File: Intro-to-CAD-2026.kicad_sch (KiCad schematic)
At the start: 6 parts

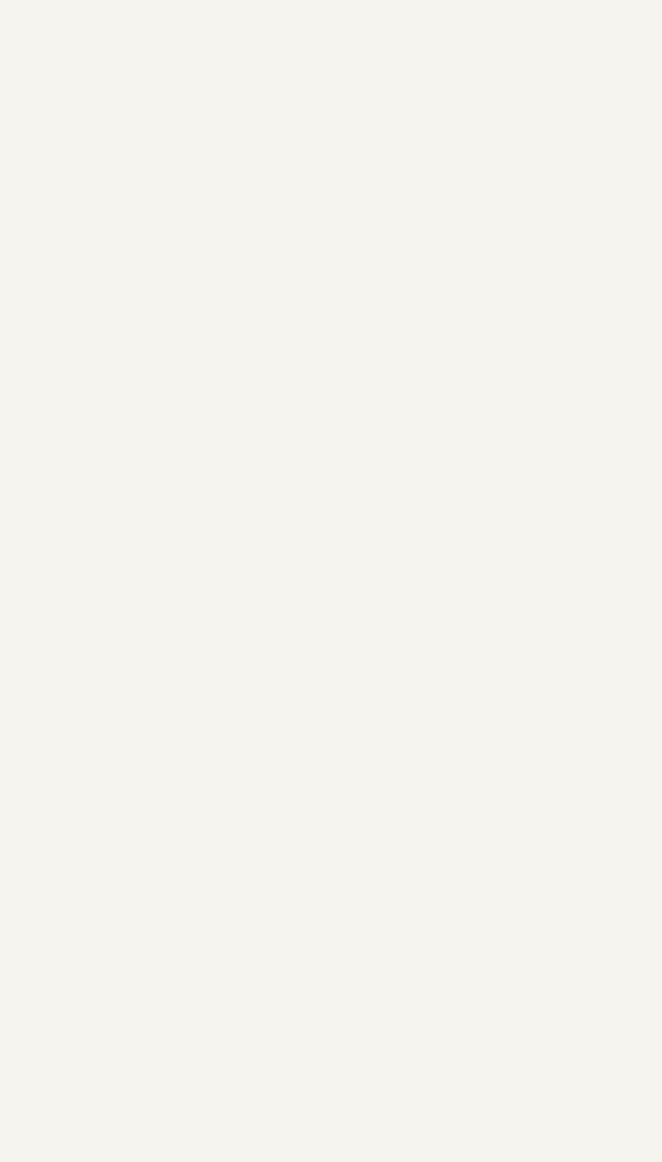
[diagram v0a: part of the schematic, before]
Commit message: Added module schematics.
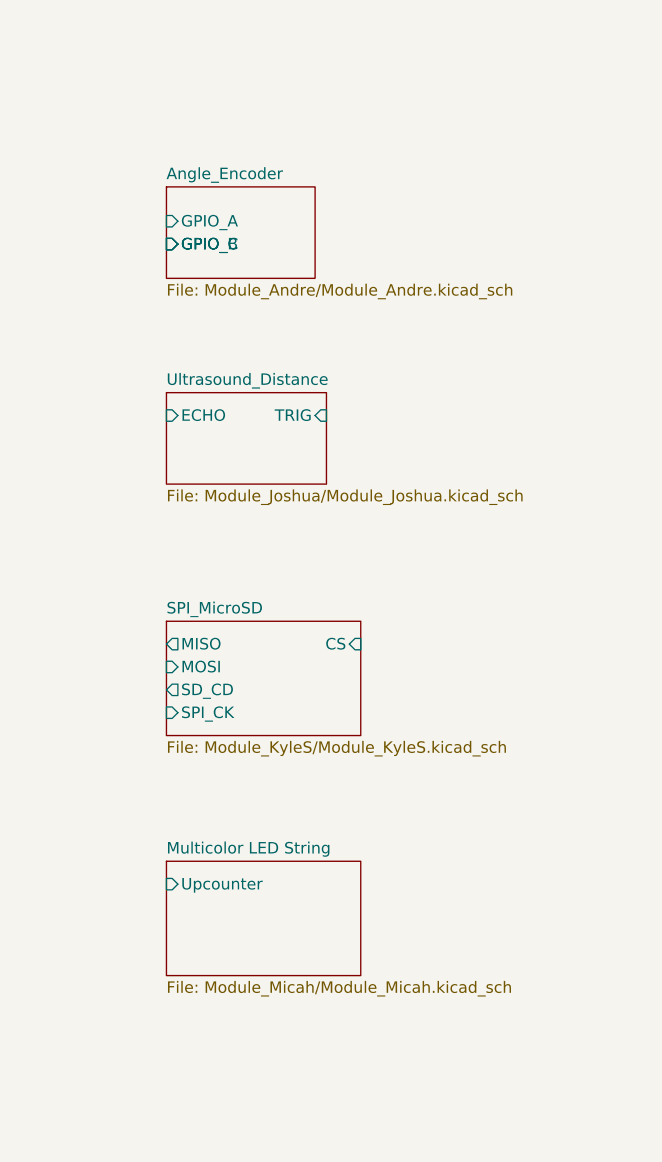
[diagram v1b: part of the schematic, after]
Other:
- added sheet Angle_Encoder (Module_Andre/Module_Andre.kicad_sch)
- added sheet Multicolor LED String (Module_Micah/Module_Micah.kicad_sch)
- added sheet SPI_MicroSD (Module_KyleS/Module_KyleS.kicad_sch)
- added sheet Ultrasound_Distance (Module_Joshua/Module_Joshua.kicad_sch)

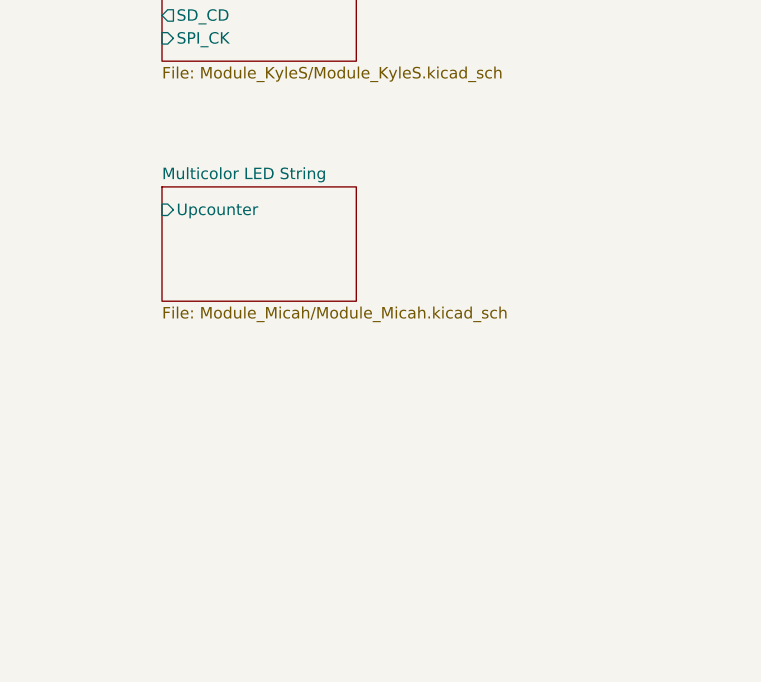
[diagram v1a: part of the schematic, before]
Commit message: Imported Student Parts
Not using Project Instances yet.
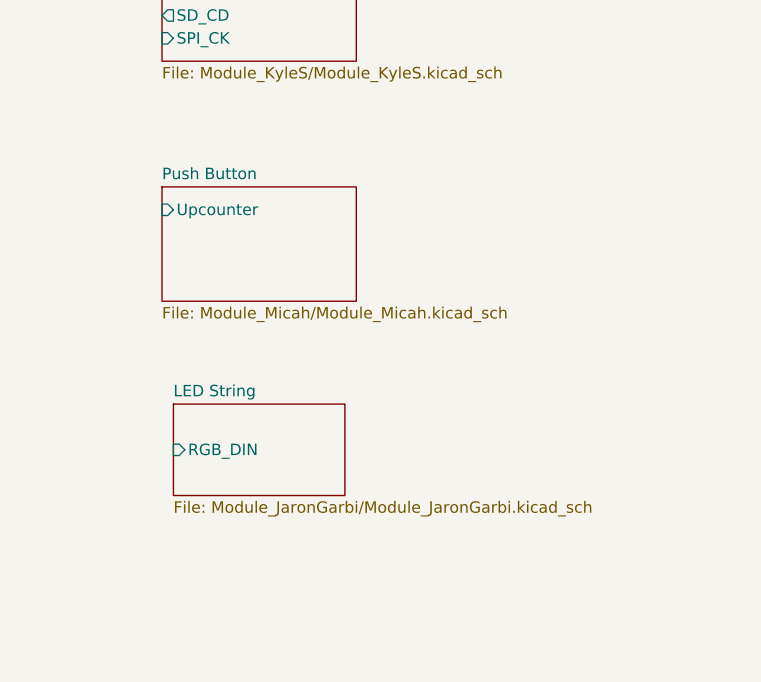
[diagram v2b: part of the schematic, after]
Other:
- sheet Multicolor LED String renamed Push Button
- added sheet LED String (Module_JaronGarbi/Module_JaronGarbi.kicad_sch)
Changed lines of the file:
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@@
+	)
+	(sheet
+		(at 125.73 138.43)
+		(size 19.05 10.16)
+		(exclude_from_sim no)
+		(in_bom yes)
+		(on_board yes)
+		(dnp no)
+		(fields_autoplaced yes)
+		(stroke
+			(width 0.1524)
+			(type solid)
+		)
+		(fill
+			(color 0 0 0 0.0000)
+		)
+		(property "Sheetname" "LED String"
+			(at 125.73 137.7184 0)
+			(effects
+				(font
+					(size 1.27 1.27)
+				)
+				(justify left bottom)
+			)
+		)
+		(property "Sheetfile" "Module_JaronGarbi/Module_JaronGarbi.kicad_sch"
+			(at 125.73 149.1746 0)
+			(effects
+				(font
+					(size 1.27 1.27)
+				)
+				(justify left top)
+			)
+		)
+		(pin "RGB_DIN" input
+			(at 125.73 143.51 180)
+			(effects
+				(font
+					(size 1.27 1.27)
+				)
+				(justify left)
+			)
+		)
+		(instances
+			(project "Intro-to-CAD-2026"
+				(path "/c12dc015-e6cb-468c-8de4-269c3106de0e"
+					(page "13")
+				)
+			)
+		)
 	)
 	(sheet
@@
 			(color 0 0 0 0.0000)
 		)
-		(property "Sheetname" "Multicolor LED String"
+		(property "Sheetname" "Push Button"
 			(at 124.46 113.5884 0)
 			(effects

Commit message: Going to school.
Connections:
- no-connect marks 19 -> 13
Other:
- added sheet OLED (oled.kicad_sch)
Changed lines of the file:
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@@
 	)
 	(no_connect
-		(at 57.15 27.94)
-	)
-	(no_connect
-		(at 57.15 25.4)
-	)
-	(no_connect
 		(at 86.36 44.45)
 	)
 	(no_connect
-		(at 57.15 35.56)
-	)
-	(no_connect
-		(at 57.15 30.48)
-	)
-	(no_connect
 		(at 86.36 52.07)
 	)
 	(no_connect
-		(at 57.15 33.02)
+		(at 146.05 92.71)
 	)
 	(no_connect
@@
 	)
 	(no_connect
-		(at 57.15 40.64)
-	)
-	(no_connect
 		(at 86.36 39.37)
 	)
@@
 	)
 	(no_connect
-		(at 57.15 38.1)
-	)
-	(no_connect
 		(at 86.36 41.91)
 	)
@@
 		)
 	)
+	(label "CS"
+		(at 57.15 27.94 180)
+		(effects
+			(font
+				(size 1.27 1.27)
+			)
+			(justify right bottom)
+		)
+	)
 	(label "OSC_SCL"
 		(at 25.4 58.42 180)
@@
 		)
 	)
+	(label "CS"
+		(at 124.46 95.25 180)
+		(effects
+			(font
+				(size 1.27 1.27)
+			)
+			(justify right bottom)
+		)
+	)
 	(label "Q_CLK"
 		(at 62.23 120.65 180)
@@
 		)
 	)
+	(label "MISO"
+		(at 124.46 90.17 180)
+		(effects
+			(font
+				(size 1.27 1.27)
+			)
+			(justify right bottom)
+		)
+	)
 	(label "MCLK"
 		(at 57.15 45.72 180)
@@
 		)
 	)
+	(label "MOSI"
+		(at 57.15 33.02 180)
+		(effects
+			(font
+				(size 1.27 1.27)
+			)
+			(justify right bottom)
+		)
+	)
 	(label "I_CLK"
 		(at 82.55 158.75 0)
@@
 		)
 	)
+	(label "SPI_CK"
+		(at 57.15 30.48 180)
+		(effects
+			(font
+				(size 1.27 1.27)
+			)
+			(justify right bottom)
+		)
+	)
 	(label "SDA"
 		(at 39.37 72.39 180)
@@
 		)
 	)
+	(label "MOSI"
+		(at 124.46 92.71 180)
+		(effects
+			(font
+				(size 1.27 1.27)
+			)
+			(justify right bottom)
+		)
+	)
 	(label "SDIN"
 		(at 57.15 43.18 180)
@@
 		)
 	)
+	(label "SPI_CK"
+		(at 124.46 97.79 180)
+		(effects
+			(font
+				(size 1.27 1.27)
+			)
+			(justify right bottom)
+		)
+	)
 	(label "OSC_SCL"
 		(at 62.23 165.1 180)
@@
 		)
 	)
+	(label "MISO"
+		(at 57.15 25.4 180)
+		(effects
+			(font
+				(size 1.27 1.27)
+			)
+			(justify right bottom)
+		)
+	)
 	(label "LRCK"
 		(at 62.23 138.43 180)
@@
 		)
 		(pin "CS" input
-			(at 146.05 90.17 0)
+			(at 124.46 95.25 180)
 			(effects
 				(font
 					(size 1.27 1.27)
 				)
-				(justify right)
+				(justify left)
 			)
 		)
@@
 		)
 		(pin "SD_CD" output
-			(at 124.46 95.25 180)
+			(at 146.05 92.71 0)
 			(effects
 				(font
 					(size 1.27 1.27)
 				)
-				(justify left)
+				(justify right)
 			)
 		)
@@
 		)
 		(pin "TRIG" input
-			(at 142.24 64.77 0)
+			(at 124.46 67.31 180)
 			(effects
 				(font
 					(size 1.27 1.27)
 				)
-				(justify right)
+				(justify left)
 			)
 		)
@@
 				)
 			)
+		)
+	)
+	(sheet
+		(at 173.355 91.44)
+		(size 24.765 13.97)
+		(exclude_from_sim no)
+		(in_bom yes)
+		(on_board yes)
+		(dnp no)
+		(fields_autoplaced yes)
+		(stroke
+			(width 0.1524)
+			(type solid)
+		)
+		(fill
+			(color 0 0 0 0.0000)
+		)
+		(property "Sheetname" "OLED"
+			(at 173.355 90.7284 0)
+			(effects
+				(font
+					(size 1.27 1.27)
+				)
+				(justify left bottom)
+			)
+		)
+		(property "Sheetfile" "oled.kicad_sch"
+			(at 173.355 105.9946 0)
+			(effects
+				(font
+					(size 1.27 1.27)
+				)
+				(justify left top)
+			)
+		)
+		(instances
+			(project "Intro-to-CAD-2026"
+				(path "/c12dc015-e6cb-468c-8de4-269c3106de0e"
+					(page "14")
+				)
+			)

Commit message: No Errors No Warnings
Some were excluded.
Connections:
- no-connect marks 13 -> 7
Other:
- sheet OLED ports: added SCL, SDA; removed none
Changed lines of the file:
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@@
 	)
 	(no_connect
-		(at 86.36 59.69)
-	)
-	(no_connect
-		(at 86.36 49.53)
+		(at 57.15 40.64)
 	)
 	(no_connect
@@
 	)
 	(no_connect
-		(at 86.36 52.07)
-	)
-	(no_connect
-		(at 146.05 92.71)
-	)
-	(no_connect
-		(at 86.36 54.61)
-	)
-	(no_connect
 		(at 82.55 162.56)
 	)
 	(no_connect
-		(at 86.36 46.99)
-	)
-	(no_connect
 		(at 86.36 39.37)
 	)
@@
 	)
 	(no_connect
-		(at 86.36 57.15)
-	)
-	(no_connect
 		(at 86.36 31.75)
 	)
@@
 		)
 	)
+	(label "SW_C"
+		(at 124.46 46.99 180)
+		(effects
+			(font
+				(size 1.27 1.27)
+			)
+			(justify right bottom)
+		)
+	)
 	(label "CS"
 		(at 57.15 27.94 180)
@@
 		)
 	)
+	(label "SCL"
+		(at 124.46 166.37 180)
+		(effects
+			(font
+				(size 1.27 1.27)
+			)
+			(justify right bottom)
+		)
+	)
+	(label "ANG_A"
+		(at 124.46 41.91 180)
+		(effects
+			(font
+				(size 1.27 1.27)
+			)
+			(justify right bottom)
+		)
+	)
 	(label "OSC_SCL"
 		(at 25.4 58.42 180)
@@
 		)
 	)
+	(label "SDA"
+		(at 124.46 163.83 180)
+		(effects
+			(font
+				(size 1.27 1.27)
+			)
+			(justify right bottom)
+		)
+	)
 	(label "I_CLK"
 		(at 62.23 118.11 180)
@@
 		)
 	)
+	(label "RGB_DIN"
+		(at 86.36 46.99 0)
+		(effects
+			(font
+				(size 1.27 1.27)
+			)
+			(justify left bottom)
+		)
+	)
+	(label "ANG_B"
+		(at 124.46 44.45 180)
+		(effects
+			(font
+				(size 1.27 1.27)
+			)
+			(justify right bottom)
+		)
+	)
 	(label "DATA"
 		(at 57.15 60.96 180)
@@
 		)
 	)
+	(label "TRIG"
+		(at 86.36 54.61 0)
+		(effects
+			(font
+				(size 1.27 1.27)
+			)
+			(justify left bottom)
+		)
+	)
 	(label "CS"
 		(at 124.46 95.25 180)
@@
 		)
 	)
+	(label "SW_C"
+		(at 57.15 38.1 180)
+		(effects
+			(font
+				(size 1.27 1.27)
+			)
+			(justify right bottom)
+		)
+	)
 	(label "Q"
 		(at 62.23 184.15 180)
@@
 		)
 	)
+	(label "ANG_A"
+		(at 86.36 57.15 0)
+		(effects
+			(font
+				(size 1.27 1.27)
+			)
+			(justify left bottom)
+		)
+	)
+	(label "ANG_B"
+		(at 86.36 59.69 0)
+		(effects
+			(font
+				(size 1.27 1.27)
+			)
+			(justify left bottom)
+		)
+	)
 	(label "MOSI"
 		(at 57.15 33.02 180)
@@
 		)
 	)
+	(label "ECHO"
+		(at 124.46 64.77 180)
+		(effects
+			(font
+				(size 1.27 1.27)
+			)
+			(justify right bottom)
+		)
+	)
 	(label "I_CLK"
 		(at 82.55 158.75 0)
@@
 		)
 	)
+	(label "RGB_DIN"
+		(at 125.73 143.51 180)
+		(effects
+			(font
+				(size 1.27 1.27)
+			)
+			(justify right bottom)
+		)
+	)
 	(label "MOSI"
 		(at 124.46 92.71 180)
@@
 		)
 	)
+	(label "BTN"
+		(at 86.36 49.53 0)
+		(effects
+			(font
+				(size 1.27 1.27)
+			)
+			(justify left bottom)
+		)
+	)
 	(label "LRCK"
 		(at 57.15 48.26 180)
@@
 		)
 	)
+	(label "SD_CD"
+		(at 57.15 35.56 180)
+		(effects
+			(font
+				(size 1.27 1.27)
+			)
+			(justify right bottom)
+		)
+	)
 	(label "I"
 		(at 62.23 181.61 180)
@@
 		)
 	)
+	(label "SD_CD"
+		(at 146.05 92.71 0)
+		(effects
+			(font
+				(size 1.27 1.27)
+			)
+			(justify left bottom)
+		)
+	)
 	(label "MISO"
 		(at 57.15 25.4 180)
@@
 		)
 	)
+	(label "BTN"
+		(at 124.46 119.38 180)
+		(effects
+			(font
+				(size 1.27 1.27)
+			)
+			(justify right bottom)
+		)
+	)
+	(label "TRIG"
+		(at 124.46 67.31 180)
+		(effects
+			(font
+				(size 1.27 1.27)
+			)
+			(justify right bottom)
+		)
+	)
 	(label "BCK"
 		(at 82.55 185.42 0)
@@
 		)
 	)
+	(label "ECHO"
+		(at 86.36 52.07 0)
+		(effects
+			(font
+				(size 1.27 1.27)
+			)
+			(justify left bottom)
+		)
+	)
 	(label "MD1"
 		(at 57.15 53.34 180)
@@
 			)
 		)
-		(pin "GPIO_A" input
-			(at 124.46 43.18 180)
+		(pin "GPIO_A" output
+			(at 124.46 41.91 180)
 			(effects
 				(font
@@
 			)
 		)
-		(pin "GPIO_B" input
-			(at 124.46 45.72 180)
+		(pin "GPIO_B" output
+			(at 124.46 44.45 180)
 			(effects
 				(font
@@
 			)
 		)
-		(pin "GPIO_C" input
-			(at 124.46 45.72 180)
+		(pin "GPIO_C" output
+			(at 124.46 46.99 180)
 			(effects
 				(font
@@
 			)
 		)
-		(pin "ECHO" input
-			(at 124.46 64.77 180)
+		(pin "TRIG" input
+			(at 124.46 67.31 180)
 			(effects
 				(font
@@
 			)
 		)
-		(pin "TRIG" input
-			(at 124.46 67.31 180)
+		(pin "ECHO" output
+			(at 124.46 64.77 180)
 			(effects
 				(font
@@
 			)
 		)
-		(pin "LRCK" input
-			(at 62.23 138.43 180)
+		(pin "SDIN" input
+			(at 62.23 146.05 180)
 			(effects
 				(font
@@
 			)
 		)
-		(pin "MCLK" input
-			(at 62.23 140.97 180)
+		(pin "LRCK" output
+			(at 62.23 138.43 180)
 			(effects
 				(font
@@
 			)
 		)
-		(pin "SCLK" input
-			(at 62.23 143.51 180)
+		(pin "MCLK" output
+			(at 62.23 140.97 180)
 			(effects
 				(font
@@
 			)
 		)
-		(pin "SDIN" input
-			(at 62.23 146.05 180)
+		(pin "SCLK" input
+			(at 62.23 143.51 180)
 			(effects
 				(font
@@
 	)
 	(sheet
-		(at 173.355 91.44)
-		(size 24.765 13.97)
+		(at 124.46 157.48)
+		(size 24.13 13.97)
 		(exclude_from_sim no)
 		(in_bom yes)
@@
 		)
 		(property "Sheetname" "OLED"
-			(at 173.355 90.7284 0)
+			(at 124.46 156.7684 0)
 			(effects
 				(font
@@
 		)
 		(property "Sheetfile" "oled.kicad_sch"
-			(at 173.355 105.9946 0)
+			(at 124.46 172.0346 0)
 			(effects
 				(font
@@
 			)
 		)
+		(pin "SCL" input
+			(at 124.46 166.37 180)
+			(effects
+				(font
+					(size 1.27 1.27)
+				)
+				(justify left)
+			)
+		)
+		(pin "SDA" input
+			(at 124.46 163.83 180)
+			(effects
+				(font
+					(size 1.27 1.27)
+				)
+				(justify left)
+			)
+		)
 		(instances
 			(project "Intro-to-CAD-2026"
@@
 			)
 		)
-		(pin "Upcounter" input
-			(at 124.46 116.84 180)
+		(pin "Upcounter" output
+			(at 124.46 119.38 180)
 			(effects
 				(font

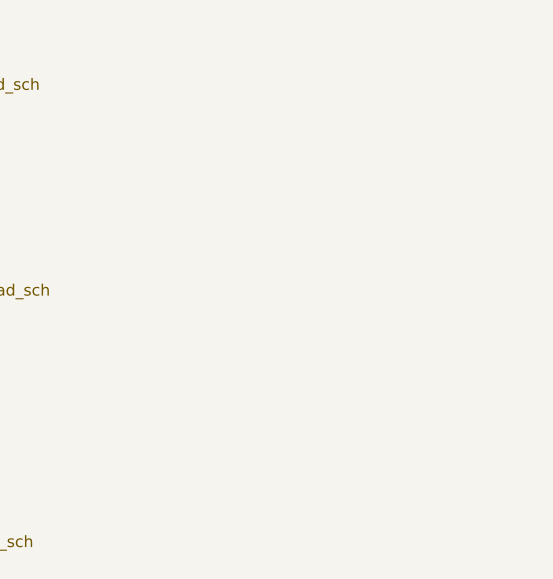
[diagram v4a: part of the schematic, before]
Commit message: Adding TC118S
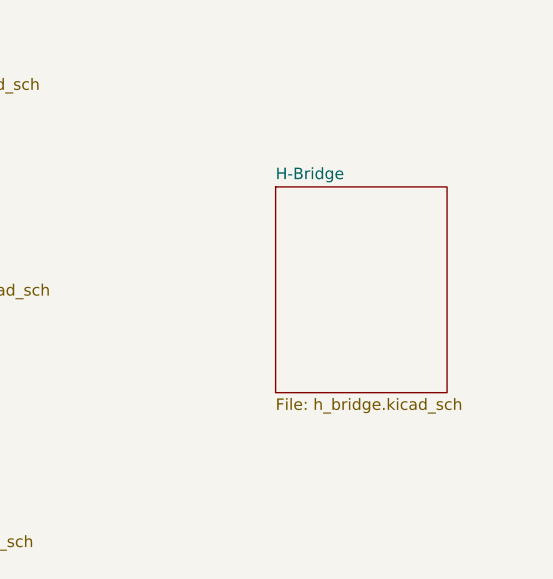
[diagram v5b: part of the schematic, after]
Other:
- added sheet H-Bridge (h_bridge.kicad_sch)
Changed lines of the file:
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@@
+	)
+	(sheet
+		(at 189.23 62.23)
+		(size 19.05 22.86)
+		(exclude_from_sim no)
+		(in_bom yes)
+		(on_board yes)
+		(dnp no)
+		(fields_autoplaced yes)
+		(stroke
+			(width 0.1524)
+			(type solid)
+		)
+		(fill
+			(color 0 0 0 0.0000)
+		)
+		(property "Sheetname" "H-Bridge"
+			(at 189.23 61.5184 0)
+			(effects
+				(font
+					(size 1.27 1.27)
+				)
+				(justify left bottom)
+			)
+		)
+		(property "Sheetfile" "h_bridge.kicad_sch"
+			(at 189.23 85.6746 0)
+			(effects
+				(font
+					(size 1.27 1.27)
+				)
+				(justify left top)
+			)
+		)
+		(instances
+			(project "Intro-to-CAD-2026"
+				(path "/c12dc015-e6cb-468c-8de4-269c3106de0e"
+					(page "15")
+				)
+			)
+		)
 	)
 	(sheet

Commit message: Added H-Bridge PCB Edits
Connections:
- no-connect marks 7 -> 5
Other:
- sheet H-Bridge ports: added INA, INB; removed none
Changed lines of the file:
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@@
 	)
 	(no_connect
-		(at 86.36 39.37)
-	)
-	(no_connect
 		(at 86.36 36.83)
 	)
 	(no_connect
-		(at 86.36 41.91)
-	)
-	(no_connect
 		(at 86.36 31.75)
 	)
@@
 		)
 	)
+	(label "INB"
+		(at 189.23 69.85 180)
+		(effects
+			(font
+				(size 1.27 1.27)
+			)
+			(justify right bottom)
+		)
+	)
 	(label "OSC_SCL"
 		(at 25.4 58.42 180)
@@
 		)
 	)
+	(label "INA"
+		(at 86.36 41.91 0)
+		(effects
+			(font
+				(size 1.27 1.27)
+			)
+			(justify left bottom)
+		)
+	)
 	(label "I_CLK"
 		(at 62.23 118.11 180)
@@
 		)
 	)
+	(label "INA"
+		(at 189.23 66.04 180)
+		(effects
+			(font
+				(size 1.27 1.27)
+			)
+			(justify right bottom)
+		)
+	)
 	(label "SPI_CK"
 		(at 124.46 97.79 180)
@@
 		)
 	)
+	(label "INB"
+		(at 86.36 39.37 0)
+		(effects
+			(font
+				(size 1.27 1.27)
+			)
+			(justify left bottom)
+		)
+	)
 	(label "ECHO"
 		(at 86.36 52.07 0)
@@
 			)
 		)
+		(pin "INA" input
+			(at 189.23 66.04 180)
+			(effects
+				(font
+					(size 1.27 1.27)
+				)
+				(justify left)
+			)
+		)
+		(pin "INB" input
+			(at 189.23 69.85 180)
+			(effects
+				(font
+					(size 1.27 1.27)
+				)
+				(justify left)
+			)
+		)
